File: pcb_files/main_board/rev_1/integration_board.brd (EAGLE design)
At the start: 22 parts, among them U1 ARDUINO-MEGAFULL

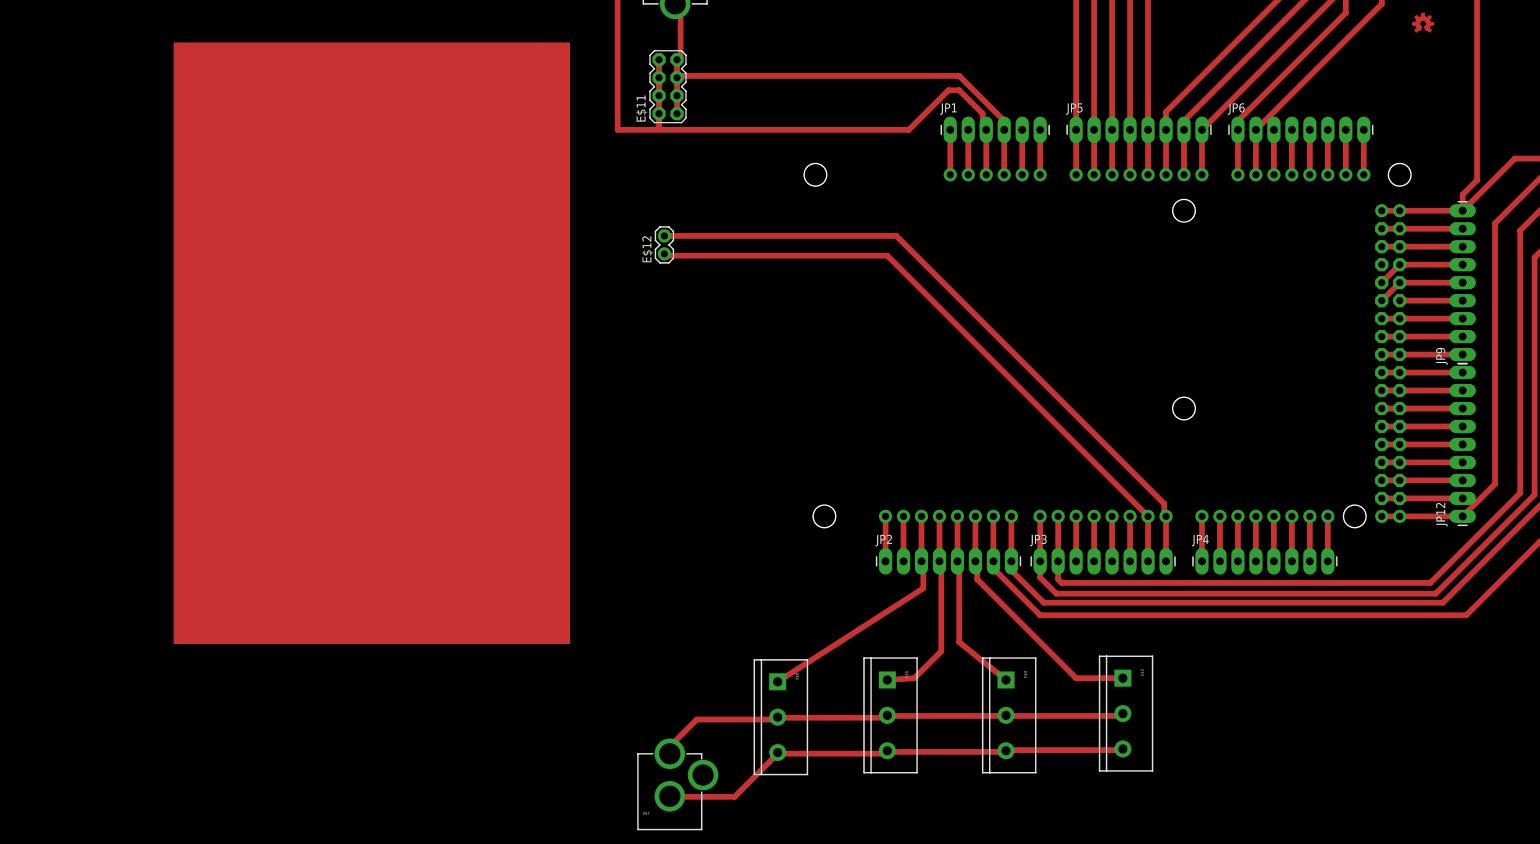
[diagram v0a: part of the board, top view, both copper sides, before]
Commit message: Added more stuff to board layout
Added leds, buttons, resistors, rerouted some wires, added some pwm for
main motor drivers
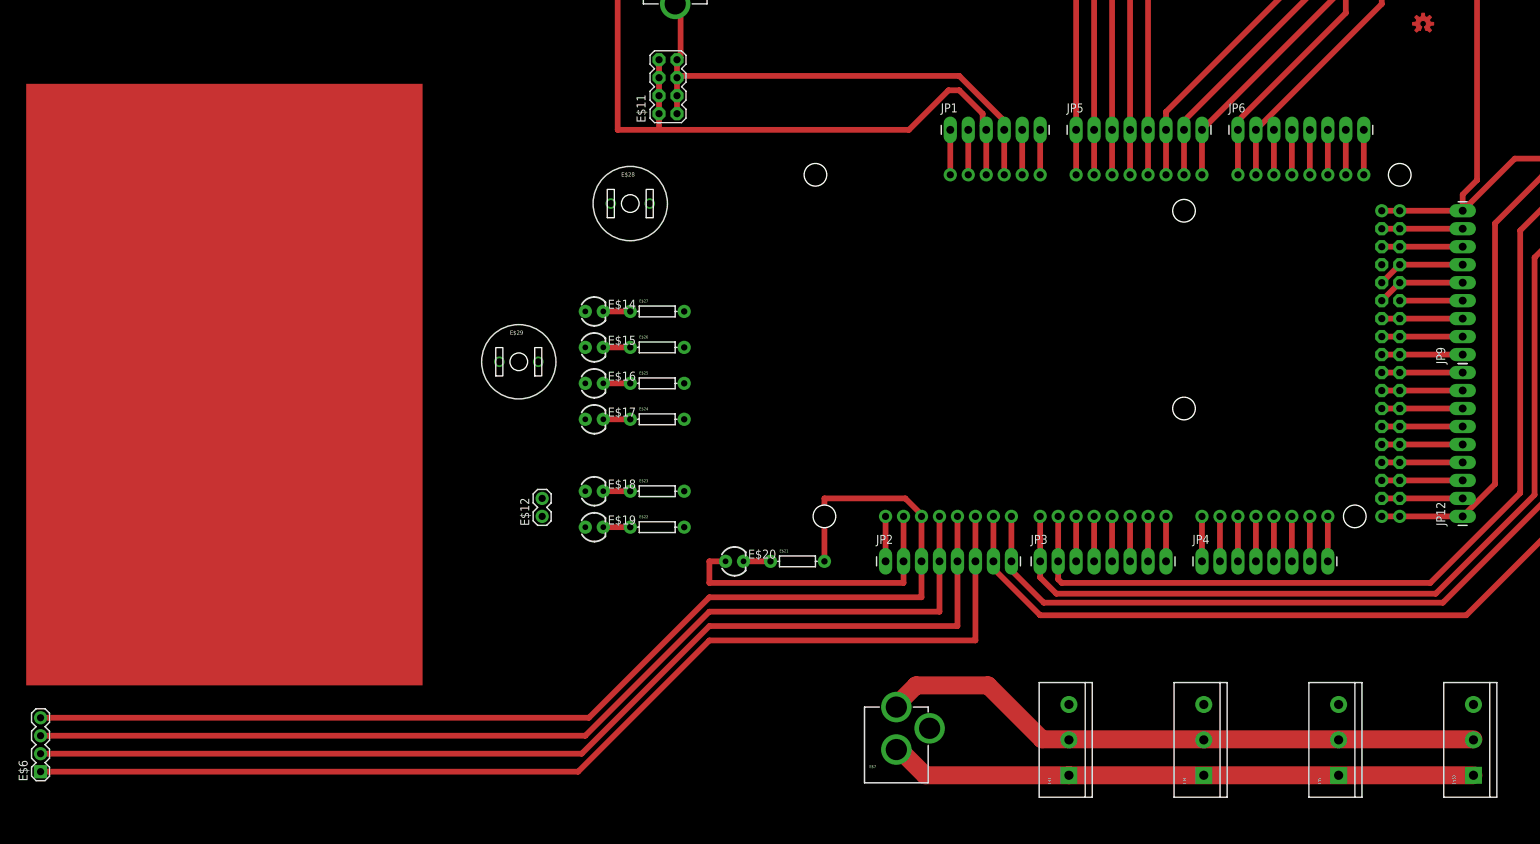
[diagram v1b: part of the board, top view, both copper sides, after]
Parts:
- added E$14, E$15, E$16, E$17, E$18, E$19, E$20: (no value), SparkFun-LED:LED3MM
- added E$21, E$22, E$23, E$24, E$25, E$26, E$27: (no value), SparkFun-Resistors:AXIAL-0.3
- added E$28, E$29: (no value), SparkFun-Electromechanical:BUTTON-10MM
- added E$30: (no value), SparkFun-Connectors:SCREWTERMINAL-5MM-3
- E$6: device SparkFun-Connectors:SCREWTERMINAL-5MM-3 -> SparkFun-Connectors:1X04
- moved E$6 104.9 mm to (-212.3, -32.3), turned to 90 degrees
- moved E$5 65.2 mm to (-29.0, -32.8), turned to 90 degrees
- moved E$12 40.9 mm to (-141.5, 3.81)
- moved E$7 32.7 mm to (-91.4, -36.8)
- moved E$4 31.0 mm to (-48.0, -32.8), turned to 90 degrees
- moved E$3 15.7 mm to (-67.1, -32.8), turned to 90 degrees
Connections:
- removed net S$28: E$3.1, JP2.6, U1.10
- removed net S$38: E$12.2
- new net S$65: E$6.3, JP2.4, U1.12
- new net S$74: E$14.K, E$27.P$1
- new net S$75: E$15.K, E$26.P$1
- new net S$76: E$16.K, E$25.P$1
- new net S$77: E$17.K, E$24.P$1
- new net S$78: E$18.K, E$23.P$1
- new net S$79: E$19.K, E$22.P$1
- new net S$80: E$20.K, E$21.P$1
- new net S$81: E$21.P$2
- new net S$82: E$6.1, JP2.6, U1.10
- net S$24: now also E$20.A
- net S$25: now also E$6.4; no longer E$6.1
- net S$26: now also E$3.1, E$30.1; no longer E$5.1, JP2.4, U1.12
- net S$27: now also E$6.2; no longer E$4.1
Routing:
- net S$82: track 0.00 -> 157.5 mm
- net S$27: track 26.5 -> 152.8 mm
- net S$25: track 34.9 -> 143.4 mm
- net S$38: track 88.3 -> 0.72 mm
- net S$68: track 89.7 -> 6.35 mm
- net S$65: track 66.9 -> 148.0 mm
- net S$26: track 28.5 -> 82.9 mm
- net S$24: track 6.35 -> 42.4 mm
- net S$28: track 35.5 -> 0.00 mm
- net S$66: track 50.1 -> 85.5 mm
- net S$81: track 0.00 -> 23.9 mm
- net S$37: track 16.5 -> 0.00 mm
- net S$80: track 0.00 -> 3.81 mm
- net S$79: track 0.00 -> 3.81 mm
- net S$78: track 0.00 -> 3.81 mm
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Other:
- board outline added: 6.5 x 4 mm

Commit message: Added SDA/SCL pins, rerouted a lot of wires
Still not finished
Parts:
- removed E$10: (no value), SparkFun-Connectors:1X04
- removed E$12: (no value), SparkFun-Connectors:1X02
- removed E$13: (no value), SparkFun-Aesthetics:OSHW-LOGO-S_COPPER
- added PWM10-13: (no value), SparkFun-Connectors:1X04
- added SDA/SCL: (no value), SparkFun-Connectors:2X3
- added TX1/RX1: (no value), SparkFun-Connectors:1X02
- moved E$6 235.0 mm to (11.4, 39.4)
- moved E$9 43.4 mm to (11.4, 3.81)
- moved E$11 30.7 mm to (-93.2, 68.1)
- moved E$28 24.3 mm to (-109.7, 62.7)
- moved E$29 23.9 mm to (-128.3, 42.9)
- moved E$18 21.2 mm to (-132.3, -13.7), turned to 90 degrees
- moved E$19 17.4 mm to (-127.3, -13.7), turned to 90 degrees
- moved E$23 14.1 mm to (-132.3, -4.83), turned to 90 degrees
- moved E$8 12.0 mm to (-111.3, 93.7)
- moved E$1 11.7 mm to (-16.8, 80.8)
- moved E$22 7.40 mm to (-127.3, -4.83), turned to 90 degrees
- moved E$2 0.80 mm to (-60.2, 80.8)
- renumbered E$20 to L13, E$21 to R13
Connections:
- removed net S$25: E$6.4, JP2.3, U1.13
- removed net S$32: E$9.2, JP3.2, U1.6
- removed net S$4: E$11.1, E$11.5, E$11.7, E$8.PWR, JP1.4, U1.GND@0
- removed net S$47: E$11.2, E$11.4, E$11.6
- removed net S$65: E$6.3, JP2.4, U1.12
- removed net S$81: R13.P$2
- removed net S$82: E$6.1, JP2.6, U1.10
- new net S$28: JP2.7, U1.9
- new net S$37: JP2.8, U1.8
- new net S$83: JP3.1, U1.7
- new net S$84: JP3.2, U1.6
- new net S$85: JP2.3, PWM10-13.4, U1.13
- net S$10: no longer E$2.4
- net S$11: no longer E$2.5
- net S$12: no longer E$1.1
- net S$13: no longer E$1.2
- net S$14: no longer E$1.3
- net S$15: no longer E$1.4
- net S$23: now also JP2.6, PWM10-13.1, U1.10; no longer JP2.1, U1.AREF
- net S$24: now also R13.P$2; no longer JP2.2, L13.A, U1.GND@4
- net S$27: now also JP2.4, PWM10-13.3, U1.12; no longer E$6.2, JP2.5, U1.11
- net S$29: now also JP2.1, U1.AREF; no longer E$10.1, JP2.7, U1.9
- net S$3: now also E$11.1, E$11.3, E$11.5, E$11.7; no longer E$8.GND
- net S$30: now also E$11.2, E$11.4, E$11.6, E$11.8, E$14.A, E$15.A, E$16.A, E$17.A, E$18.A, E$19.A, JP1.4, JP2.2, L13.A, U1.GND@0, U1.GND@4; no longer E$10.2, JP2.8, U1.8
- net S$31: now also JP2.5, PWM10-13.2, U1.11; no longer E$9.1, JP3.1, U1.7
- net S$43: now also E$22.P$2, TX1/RX1.2
- net S$44: now also E$23.P$2, TX1/RX1.1
- net S$45: now also SDA/SCL.1, SDA/SCL.5
- net S$46: now also SDA/SCL.2, SDA/SCL.6
- net S$48: now also E$24.P$2
- net S$49: now also E$25.P$2
- net S$50: now also E$26.P$2
- net S$51: now also E$27.P$2
- net S$67: no longer E$10.3, E$9.4
- net S$7: no longer E$2.1
- net S$72: no longer E$10.4, E$9.3
- net S$8: no longer E$2.2
- net S$9: no longer E$2.3
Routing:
- net S$30: track 96.7 -> 285.8 mm
- net S$82: track 157.5 -> 0.00 mm
- net S$65: track 148.0 -> 0.00 mm
- net S$23: track 6.96 -> 152.8 mm
- net S$25: track 143.4 -> 0.00 mm
- net S$85: track 0.00 -> 141.4 mm
- net S$67: track 142.4 -> 11.4 mm
- net S$32: track 127.2 -> 0.00 mm
- net S$52: track 11.4 -> 125.0 mm
- net S$51: track 11.4 -> 121.2 mm
- net S$44: track 6.35 -> 114.6 mm
- net S$50: track 11.4 -> 118.2 mm
- net S$49: track 11.4 -> 115.7 mm
- net S$48: track 11.4 -> 114.6 mm
- net S$72: track 113.9 -> 11.4 mm
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
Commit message: Finished routing wires, added outline
Drill holes still need to be added I think
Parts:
- removed PWM10-13: (no value), SparkFun-Connectors:1X04
- added E$10, E$12: (no value), SparkFun-Connectors:1X04
- moved E$29 23.4 mm to (-127.8, 19.6)
- moved E$14 12.0 mm to (-133.1, 44.7)
- moved E$15 12.0 mm to (-133.1, 39.6)
- moved E$26 12.0 mm to (-124.2, 39.6)
- moved E$27 12.0 mm to (-124.2, 44.7)
- moved E$17 12.0 mm to (-133.1, 29.5)
- moved E$24 12.0 mm to (-124.2, 29.5)
- moved E$16 12.0 mm to (-133.1, 34.5)
- moved E$25 12.0 mm to (-124.2, 34.5)
- moved E$6 7.73 mm to (3.81, 38.1)
- moved E$9 7.73 mm to (3.81, 2.54)
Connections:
- net S$15 renamed S$82
- net S$16 renamed S$81
- removed net S$30: E$11.2, E$11.4, E$11.6, E$11.8, E$14.A, E$15.A, E$16.A, E$17.A, E$18.A, E$19.A, JP1.4, JP2.2, L13.A, U1.GND@0, U1.GND@4
- removed net S$52: JP12.6, U1.30
- new net S$47: E$27.P$2, JP12.6, U1.30
- new net S$86: JP5.8, U1.A7
- new net S$87: E$10.2
- new net S$88: E$10.1
- new net S$89: E$12.4
- new net S$90: E$12.3
- new net S$91: U1.48
- new net S$95: E$10.4, E$11.1, E$11.3, E$11.5, E$11.7, E$12.1, E$6.4, E$9.3, JP1.3, U1.5V@0
- net S$12: now also E$6.3, E$9.4; no longer JP5.6, U1.A5
- net S$14: now also JP5.6, U1.A5; no longer JP5.8, U1.A7
- net S$23: no longer PWM10-13.1
- net S$27: no longer PWM10-13.3
- net S$3: now also E$10.3, E$11.2, E$11.4, E$11.6, E$11.8, E$12.2, E$14.A, E$15.A, E$16.A, E$17.A, E$18.A, E$19.A, JP1.4, JP2.2, L13.A, U1.GND@0, U1.GND@4; no longer E$11.1, E$11.3, E$11.5, E$11.7, JP1.3, U1.5V@0
- net S$31: no longer PWM10-13.2
- net S$33: now also E$9.1
- net S$34: now also E$9.2
- net S$35: now also E$6.1
- net S$36: now also E$6.2
- net S$48: no longer E$24.P$2
- net S$49: now also E$24.P$2; no longer E$25.P$2
- net S$50: now also E$25.P$2; no longer E$26.P$2
- net S$51: now also E$26.P$2; no longer E$27.P$2
- net S$85: no longer PWM10-13.4
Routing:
- net S$95: track 0.00 -> 579.8 mm
- net S$3: track 64.5 -> 523.2 mm
- net S$30: track 285.8 -> 0.36 mm
- net S$23: track 152.8 -> 6.60 mm
- net S$31: track 148.9 -> 6.60 mm
- net S$27: track 145.0 -> 6.60 mm
- net S$85: track 141.4 -> 6.86 mm
- net S$52: track 125.0 -> 0.36 mm
- net S$47: track 0.00 -> 121.2 mm
- net S$90: track 0.00 -> 120.5 mm
- net S$89: track 0.00 -> 116.9 mm
- net S$88: track 0.00 -> 114.1 mm
- net S$87: track 0.00 -> 110.9 mm
- net S$35: track 19.6 -> 116.4 mm
- net S$36: track 16.9 -> 112.9 mm
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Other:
- board size 6.5 x 4 mm -> 274.8 x 140.2 mm

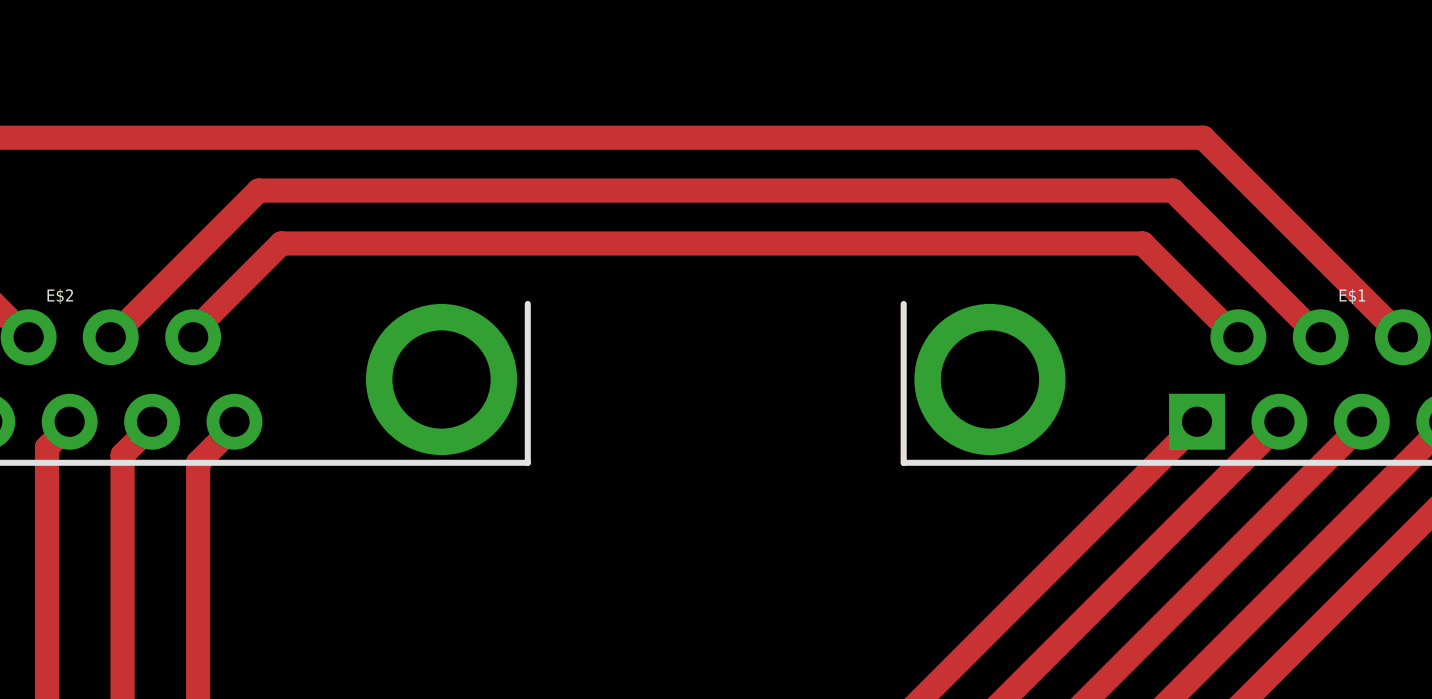
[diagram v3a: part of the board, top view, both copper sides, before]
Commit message: Edited board layout
Added I2C pins for db9s to make connecting easier. Will need a jumper
wire to connect i2c of db9s to the arduino.
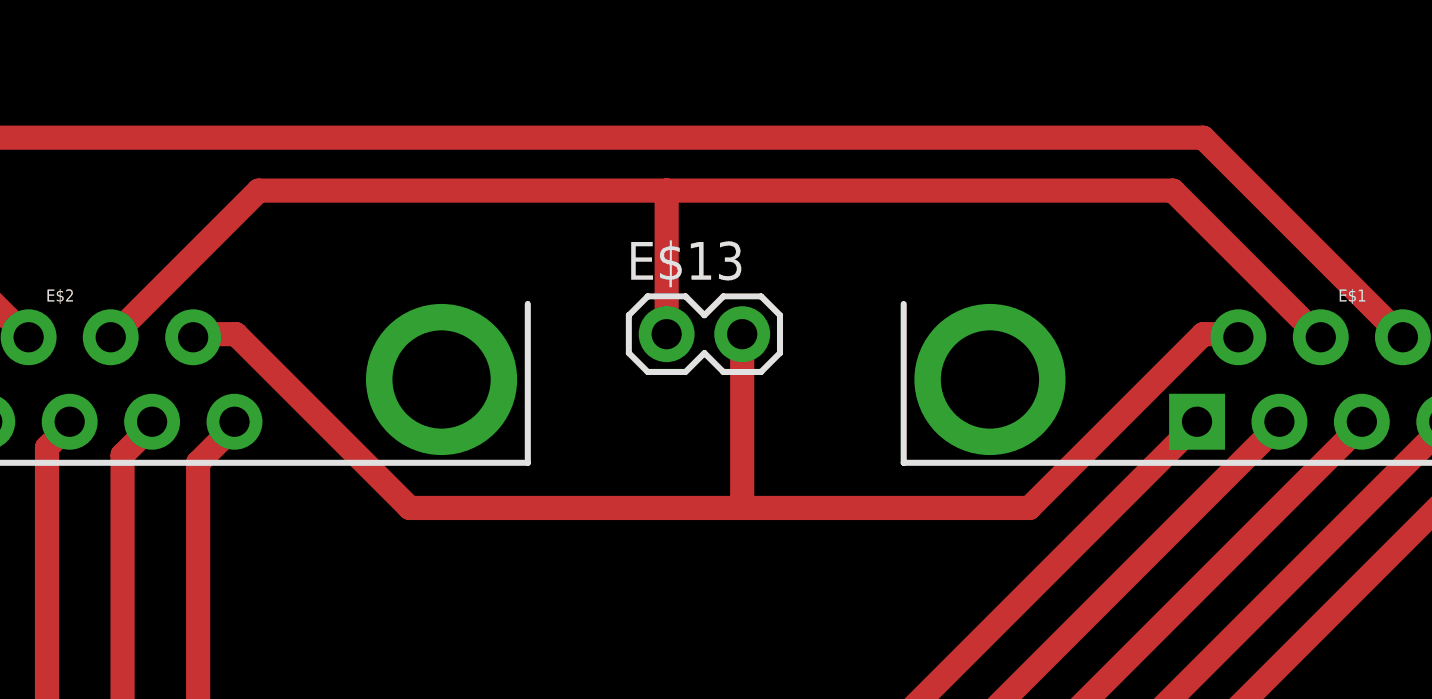
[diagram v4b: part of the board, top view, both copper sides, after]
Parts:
- added E$13: (no value), SparkFun-Connectors:1X02
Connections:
- new net S$15: E$13.1
- new net S$25: E$13.2
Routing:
- net S$25: track 0.00 -> 46.0 mm
- net S$16: track 38.4 -> 0.25 mm
- net S$15: track 45.0 -> 49.8 mm
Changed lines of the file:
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@@
 <element name="E$10" library="SparkFun-Connectors" package="1X04" value="" x="-191.262" y="-15.494" rot="R90"/>
 <element name="E$12" library="SparkFun-Connectors" package="1X04" value="" x="-191.262" y="-31.496" rot="R90"/>
+<element name="E$13" library="SparkFun-Connectors" package="1X02" value="" x="-40.132" y="82.296"/>
 </elements>
 <signals>
@@
 <signal name="S$15">
 <wire x1="-58.674" y1="82.296" x2="-53.848" y2="87.122" width="0.8128" layer="1"/>
-<wire x1="-53.848" y1="87.122" x2="-23.114" y2="87.122" width="0.8128" layer="1"/>
+<wire x1="-53.848" y1="87.122" x2="-40.132" y2="87.122" width="0.8128" layer="1"/>
+<wire x1="-40.132" y1="87.122" x2="-23.114" y2="87.122" width="0.8128" layer="1"/>
 <wire x1="-23.114" y1="87.122" x2="-18.034" y2="82.042" width="0.8128" layer="1"/>
 <wire x1="-18.034" y1="82.042" x2="-18.034" y2="82.296" width="1.27" layer="1"/>
+<contactref element="E$13" pad="1"/>
+<wire x1="-40.132" y1="82.296" x2="-40.132" y2="87.122" width="0.8128" layer="1"/>
+</signal>
+<signal name="S$25">
+<wire x1="-56.134" y1="82.042" x2="-56.134" y2="82.296" width="1.27" layer="1"/>
+<wire x1="-56.134" y1="82.296" x2="-54.61" y2="82.296" width="0.8128" layer="1"/>
+<wire x1="-54.61" y1="82.296" x2="-48.768" y2="76.454" width="0.8128" layer="1"/>
+<wire x1="-48.768" y1="76.454" x2="-37.846" y2="76.454" width="0.8128" layer="1"/>
+<wire x1="-37.592" y1="76.454" x2="-27.94" y2="76.454" width="0.8128" layer="1"/>
+<wire x1="-27.94" y1="76.454" x2="-22.098" y2="82.296" width="0.8128" layer="1"/>
+<wire x1="-22.098" y1="82.296" x2="-21.082" y2="82.296" width="0.8128" layer="1"/>
+<contactref element="E$13" pad="2"/>
+<wire x1="-37.592" y1="82.296" x2="-37.592" y2="76.454" width="0.8128" layer="1"/>
+<wire x1="-37.592" y1="76.454" x2="-37.846" y2="76.454" width="0.8128" layer="1"/>
 </signal>
 <signal name="S$16">
-<wire x1="-56.134" y1="82.296" x2="-53.086" y2="85.344" width="0.8128" layer="1"/>
-<wire x1="-53.086" y1="85.344" x2="-24.13" y2="85.344" width="0.8128" layer="1"/>
-<wire x1="-24.13" y1="85.344" x2="-20.828" y2="82.042" width="0.8128" layer="1"/>
-<wire x1="-56.134" y1="82.042" x2="-56.134" y2="82.296" width="1.27" layer="1"/>
 <wire x1="-20.828" y1="82.042" x2="-20.828" y2="82.296" width="1.27" layer="1"/>
 </signal>

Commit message: Updated Integration Board
Moved all traces to bottom layer
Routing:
- net S$37: track 45.7 -> 44.4 mm
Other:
- outline, holes or cut-outs redrawn

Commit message: Integration_board_update
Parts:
- moved E$13 9.00 mm to (-37.6, 73.7), turned to 270 degrees
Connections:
- net S$81 renamed S$97
- removed net S$15: E$13.1
- new net S$16: E$13.1
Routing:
- net S$15: track 49.8 -> 12.5 mm
- net S$16: track 0.25 -> 33.8 mm
- net S$61: track 0.25 -> 22.4 mm
- net S$3: track 523.2 -> 544.4 mm
- net S$82: track 48.6 -> 61.8 mm
- net S$25: track 46.0 -> 56.5 mm
- net S$97: track 46.8 -> 56.3 mm
- net S$86: track 50.7 -> 58.1 mm
- net S$13: track 52.8 -> 58.9 mm
- net S$14: track 52.3 -> 57.8 mm
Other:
- outline, holes or cut-outs redrawn
